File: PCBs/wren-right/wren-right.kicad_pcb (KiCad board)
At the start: 2 copper layers, 150 x 119.1 mm, 69 parts, among them J1 TRRS_Jack, SW0 Reset, U1 Elite-C

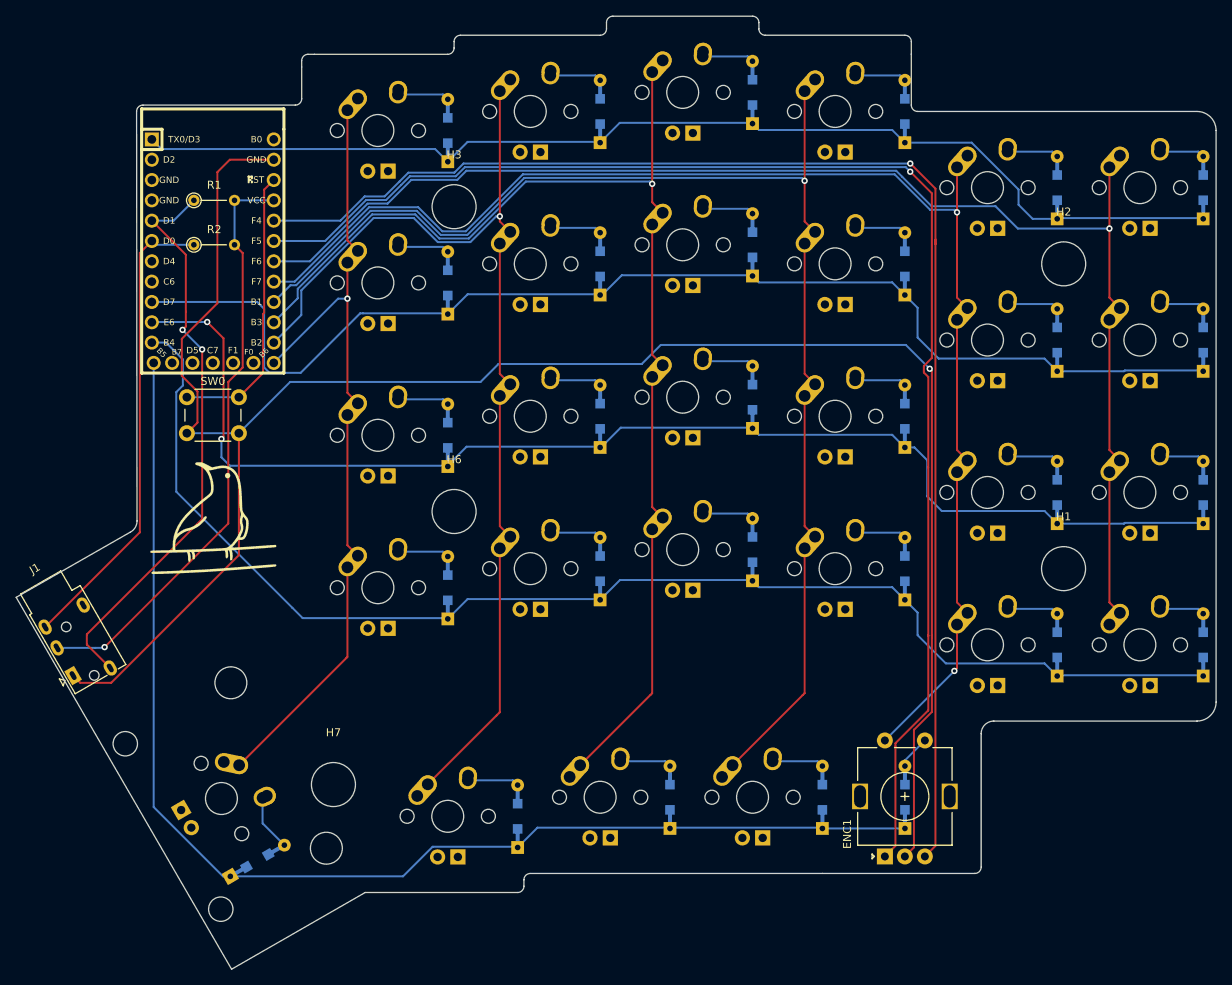
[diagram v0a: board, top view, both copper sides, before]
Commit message: Revert Kyria stagger (for now)
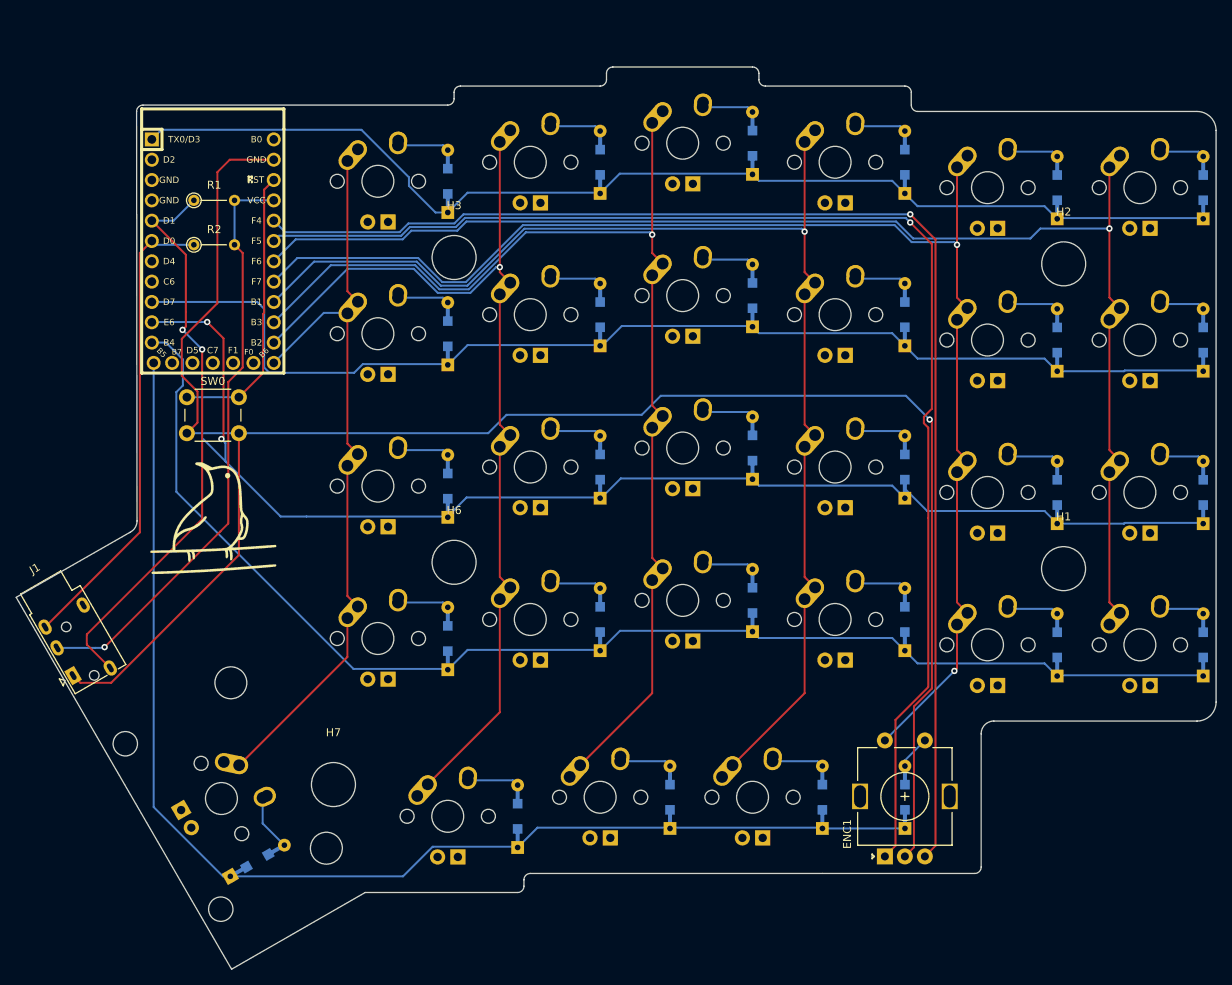
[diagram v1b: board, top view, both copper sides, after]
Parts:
- moved D13 6.35 mm to (173.0, 77.0)
- moved D21 6.35 mm to (134.9, 100.8)
- moved D23 6.35 mm to (173.0, 96.0)
- moved D31 6.35 mm to (134.9, 119.9)
- moved H3 6.35 mm to (135.7, 72.2)
- moved MX13 6.35 mm to (164.3, 77.0)
- moved MX21 6.35 mm to (126.2, 100.8)
- moved MX23 6.35 mm to (164.3, 96.0)
- moved MX31 6.35 mm to (126.2, 119.9)
- moved D2 6.35 mm to (154.0, 60.3)
- moved D3 6.35 mm to (173.0, 57.9)
- moved D4 6.35 mm to (192.1, 60.3)
- moved MX2 6.35 mm to (145.3, 60.3)
- moved MX3 6.35 mm to (164.3, 57.9)
- moved MX4 6.35 mm to (183.4, 60.3)
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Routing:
- net COL1: track 126.7 -> 115.9 mm
- net COL2: track 145.5 -> 135.9 mm
- net GND: track 247.9 -> 238.6 mm
- net LEFT: track 173.4 -> 164.2 mm
- net COL3: track 160.7 -> 151.7 mm
- net RIGHT: track 171.6 -> 163.2 mm
- net ROW1: track 151.9 -> 144.5 mm
- net COL0: track 97.4 -> 90.2 mm, vias 1 -> 0
- net COL5: track 166.5 -> 162.3 mm
- net COL4: track 168.0 -> 164.5 mm
- net ROW2: track 157.9 -> 159.7 mm
- net ROW3: track 165.4 -> 163.7 mm
- net ROW0: track 140.9 -> 141.4 mm
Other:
- board size 150 x 119.1 mm -> 150 x 112.8 mm

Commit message: Adopt Kyria-like stagger on right half
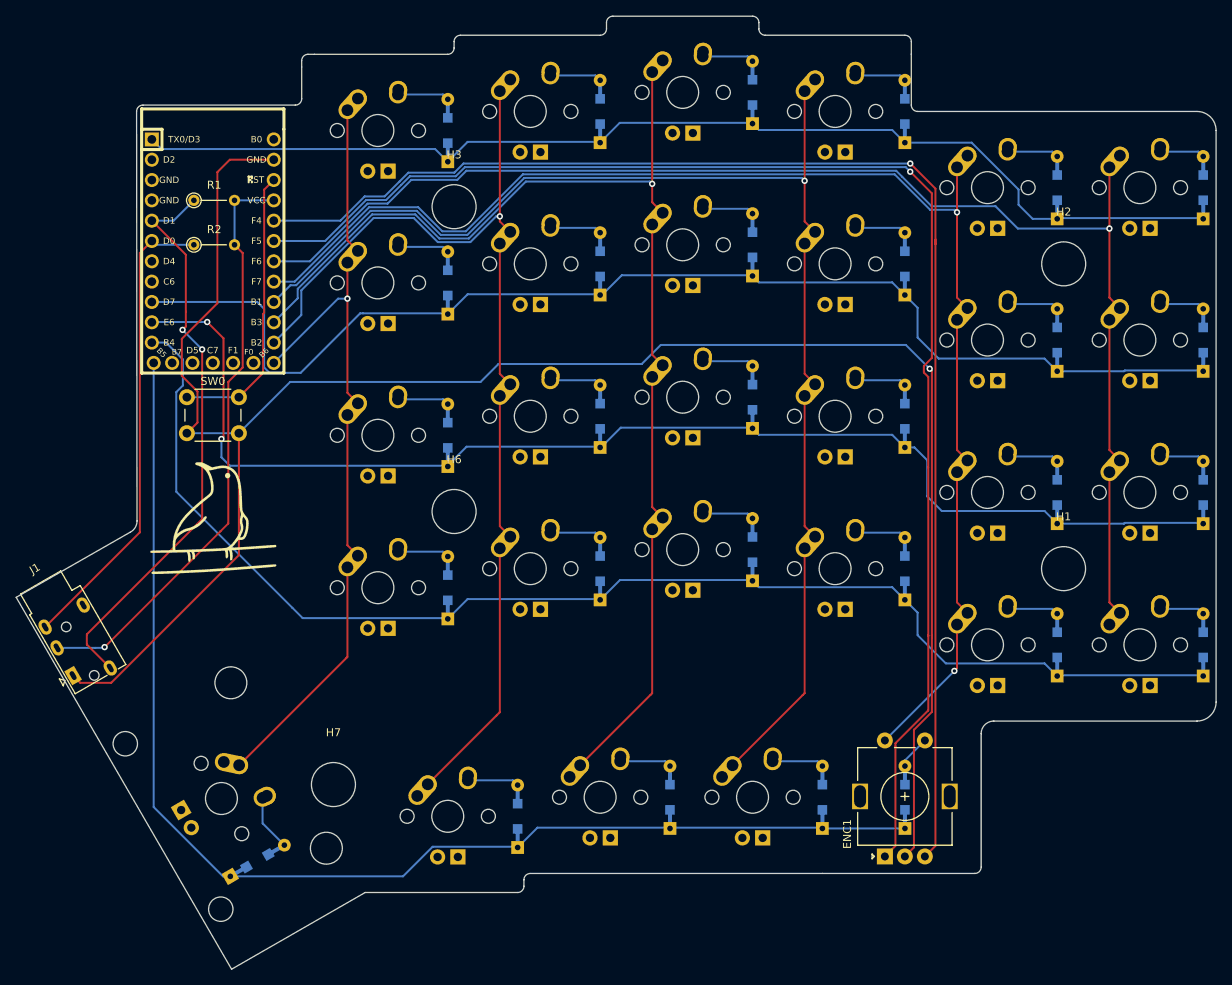
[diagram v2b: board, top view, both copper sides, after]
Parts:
- moved D13 6.35 mm to (173.0, 70.6)
- moved D21 6.35 mm to (134.9, 94.5)
- moved D23 6.35 mm to (173.0, 89.7)
- moved D31 6.35 mm to (134.9, 113.5)
- moved H3 6.35 mm to (135.7, 65.9)
- moved MX13 6.35 mm to (164.3, 70.6)
- moved MX21 6.35 mm to (126.2, 94.5)
- moved MX23 6.35 mm to (164.3, 89.7)
- moved MX31 6.35 mm to (126.2, 113.5)
- moved D2 6.35 mm to (154.0, 54.0)
- moved D3 6.35 mm to (173.0, 51.6)
- moved D4 6.35 mm to (192.1, 54.0)
- moved MX2 6.35 mm to (145.3, 54.0)
- moved MX3 6.35 mm to (164.3, 51.6)
- moved MX4 6.35 mm to (183.4, 54.0)
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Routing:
- net COL1: track 115.9 -> 126.7 mm
- net COL2: track 135.9 -> 145.5 mm
- net GND: track 238.6 -> 247.9 mm
- net LEFT: track 164.2 -> 173.4 mm
- net COL3: track 151.7 -> 160.7 mm
- net RIGHT: track 163.2 -> 171.6 mm
- net ROW1: track 144.5 -> 151.9 mm
- net COL0: track 90.2 -> 97.4 mm, vias 0 -> 1
- net COL5: track 162.3 -> 166.5 mm
- net COL4: track 164.5 -> 168.0 mm
- net ROW2: track 159.7 -> 157.9 mm
- net ROW3: track 163.7 -> 165.4 mm
- net ROW0: track 141.4 -> 140.9 mm
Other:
- board size 150 x 112.8 mm -> 150 x 119.1 mm
